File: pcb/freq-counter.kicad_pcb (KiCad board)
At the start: 4 copper layers, 152.4 x 167.6 mm, 105 parts, among them J1 RPM on board, J10 Power_T1, J11 Hz/RPM_Terminal1, J12 Hz/RPM_Terminal0, J2 BNC, J3 RPM to Board, J4 Jack-DC, J5 Segments-Terminal0, J6 Digits-Terminal0, J7 Segments-Terminal1, J8 Digits-Terminal1, J9 Power_Terminal1, Q1 CSC388A, Q10 2SC1815, Q11 2SC1815, Q12 2SC1815, Q13 2SC1815, Q14 2SC1815, Q2 CSC388A, Q3 2SA1015, Q4 2SC1815, Q5 2SC1815, Q6 CSC388A, Q7 CSC388A, Q8 CSC388A, Q9 2SC1815, SW1 on/off, SW2 count up, SW3 toggle, SW4 SW_SIGNAL, U1 SN74HC02N, U2 ATTINY4313-PU(freq-counter), U3 EE-SX460, U4 74HC00, U5 74HC00, U6 74HC00, U7 7seg-2digit-ca, U8 7seg-2digit-ca, U9 7seg-2digit-ca, Y1 10MHz

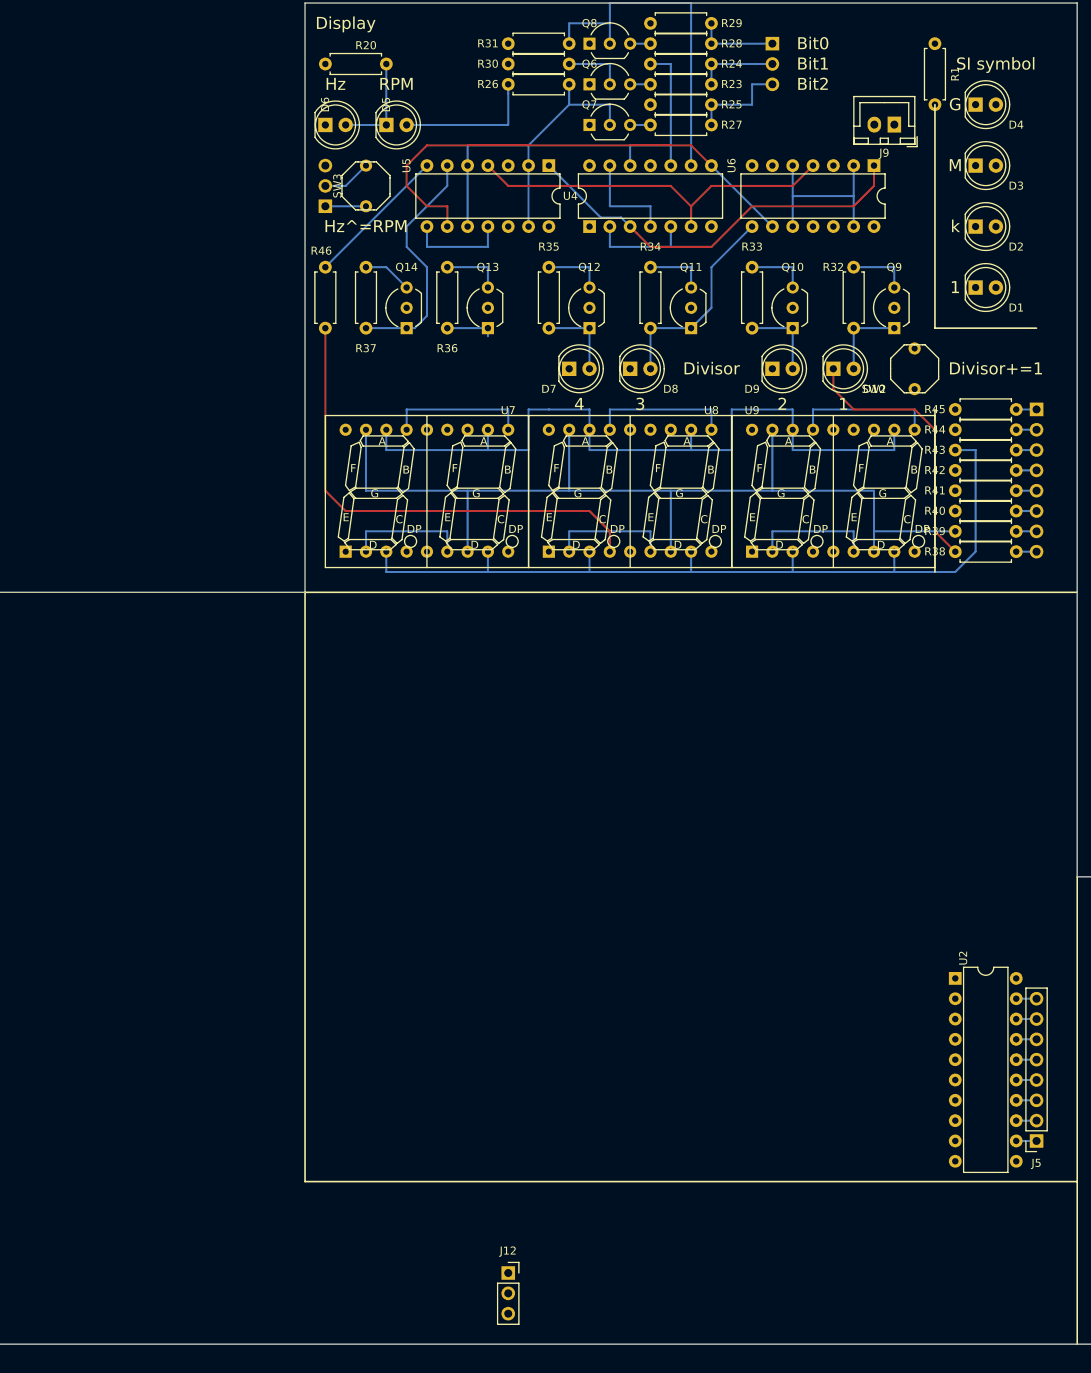
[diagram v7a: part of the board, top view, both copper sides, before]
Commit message: 1kMG-LED 部のTerminal化が完了。
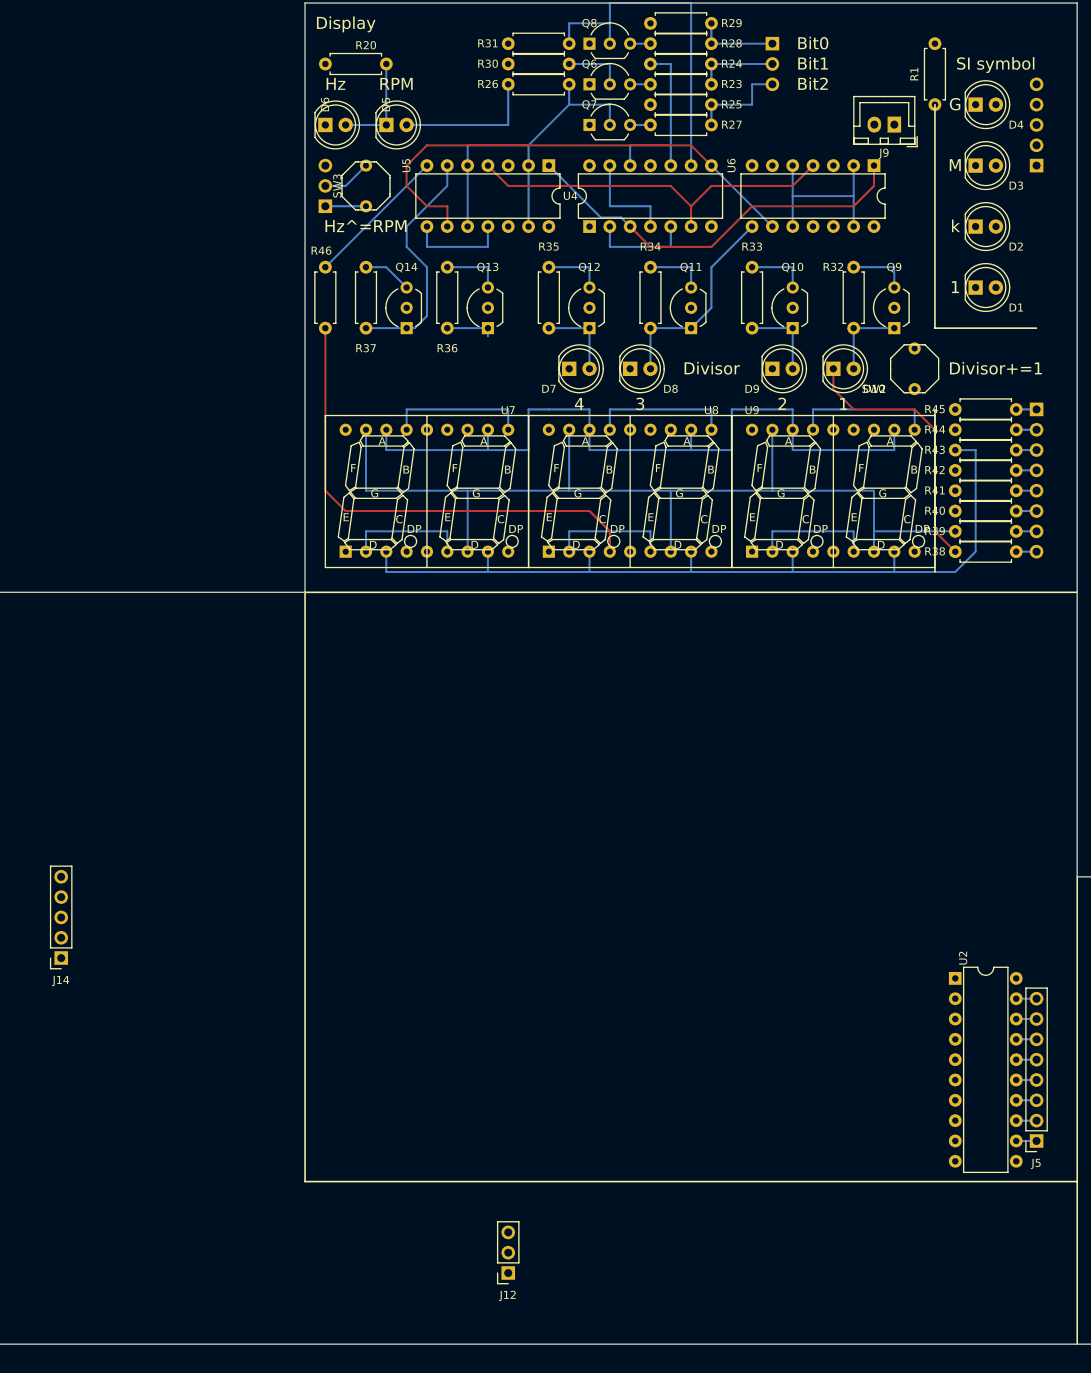
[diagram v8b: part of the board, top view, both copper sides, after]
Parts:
- added J13: 1kMG_Terminal1, Connector_PinHeader_2.54mm:PinHeader_1x05_P2.54mm_Vertical, B.Cu at (175.3, 50.8)
- added J14: 1kMG_Terminal0, Connector_PinSocket_2.54mm:PinSocket_1x05_P2.54mm_Vertical, F.Cu at (53.3, 149.9)
- moved R1 7.62 mm to (162.6, 35.6), turned to 270 degrees
- turned J12 to 180 degrees
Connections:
- R1 pad 1: Net-(D1-Pad1) -> Net-(J13-Pad5)
- R1 pad 2: GND -> Net-(D1-Pad1)
- U1 pad 1: Net-(D4-Pad2) -> /LED_G
- U1 pad 10: Net-(D1-Pad2) -> /LED_1
- U1 pad 13: Net-(D2-Pad2) -> /LED_k
- U1 pad 4: Net-(D3-Pad2) -> /LED_M
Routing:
- net Net-(D1-Pad2): track 51.9 -> 0.00 mm
- net /LED_1: track 0.00 -> 51.9 mm
- net Net-(D2-Pad2): track 46.8 -> 0.00 mm
- net /LED_k: track 0.00 -> 46.8 mm
- net Net-(D3-Pad2): track 30.0 -> 0.00 mm
- net /LED_M: track 0.00 -> 30.0 mm
- net Net-(D4-Pad2): track 27.9 -> 0.00 mm
- net /LED_G: track 0.00 -> 27.9 mm
